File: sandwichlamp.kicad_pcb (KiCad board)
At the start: 2 copper layers, 96 x 96 mm, 17 parts, among them J1 Pole1, J2 Pole2, J3 Pole3, J4 12V Enable, J5 HLK-LD2410C, SW1 Rader Power, SW3 POWER, U1 magnetic-charger, U3 hw357, U4 RX480E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

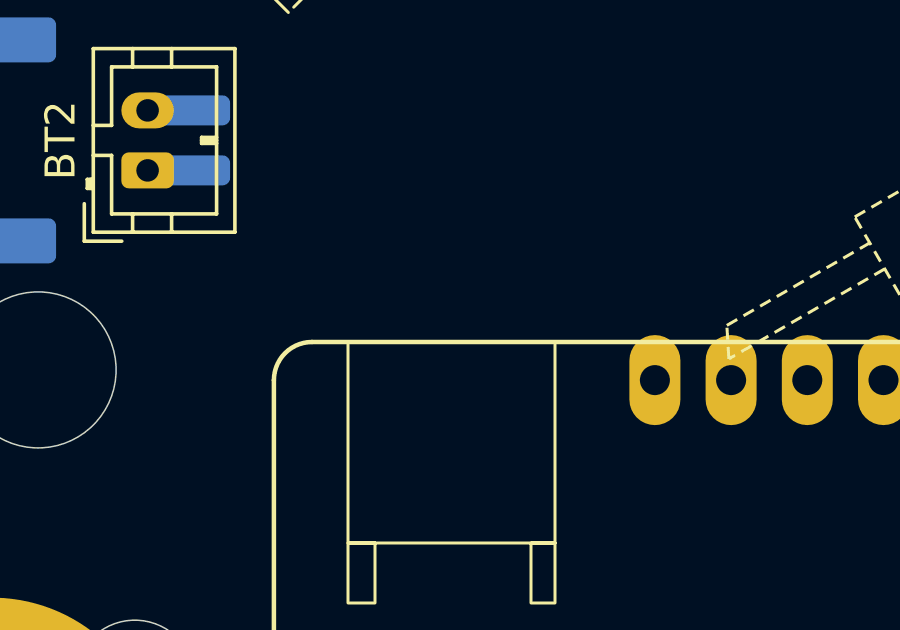
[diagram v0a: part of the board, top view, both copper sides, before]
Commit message: Add battery pad to the Lolin where the battery voltage can be taken for the ESP
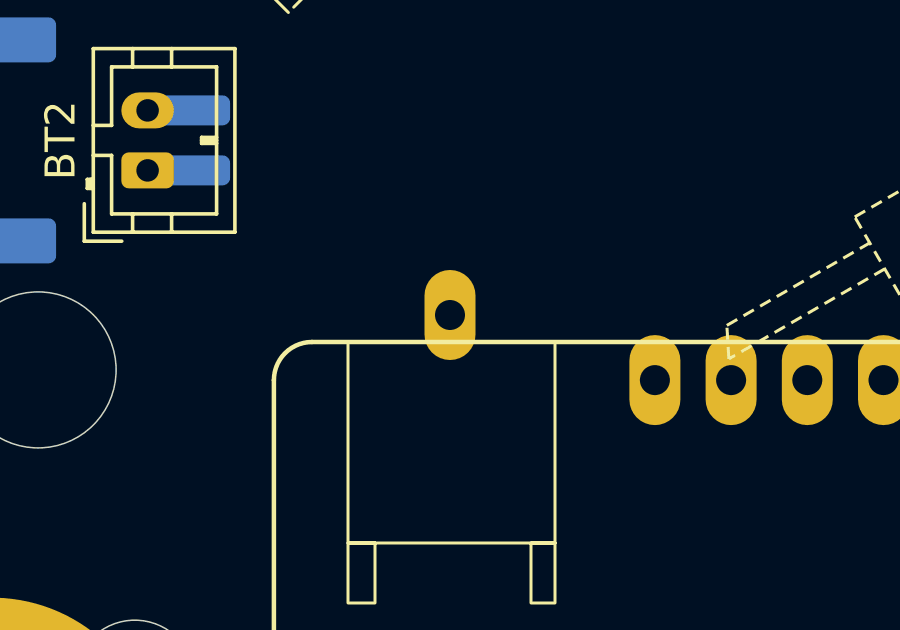
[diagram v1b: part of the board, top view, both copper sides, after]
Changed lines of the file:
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@@
 			(pintype "bidirectional")
+		)
+		(pad "37" thru_hole oval
+			(at -13.6 20.8 270)
+			(size 3 1.7)
+			(drill 1)
+			(layers "*.Cu" "*.Mask")
+			(remove_unused_layers no)
 		)
 		(model "${KIPRJMOD}/lib/lolin32/lolin32.step"

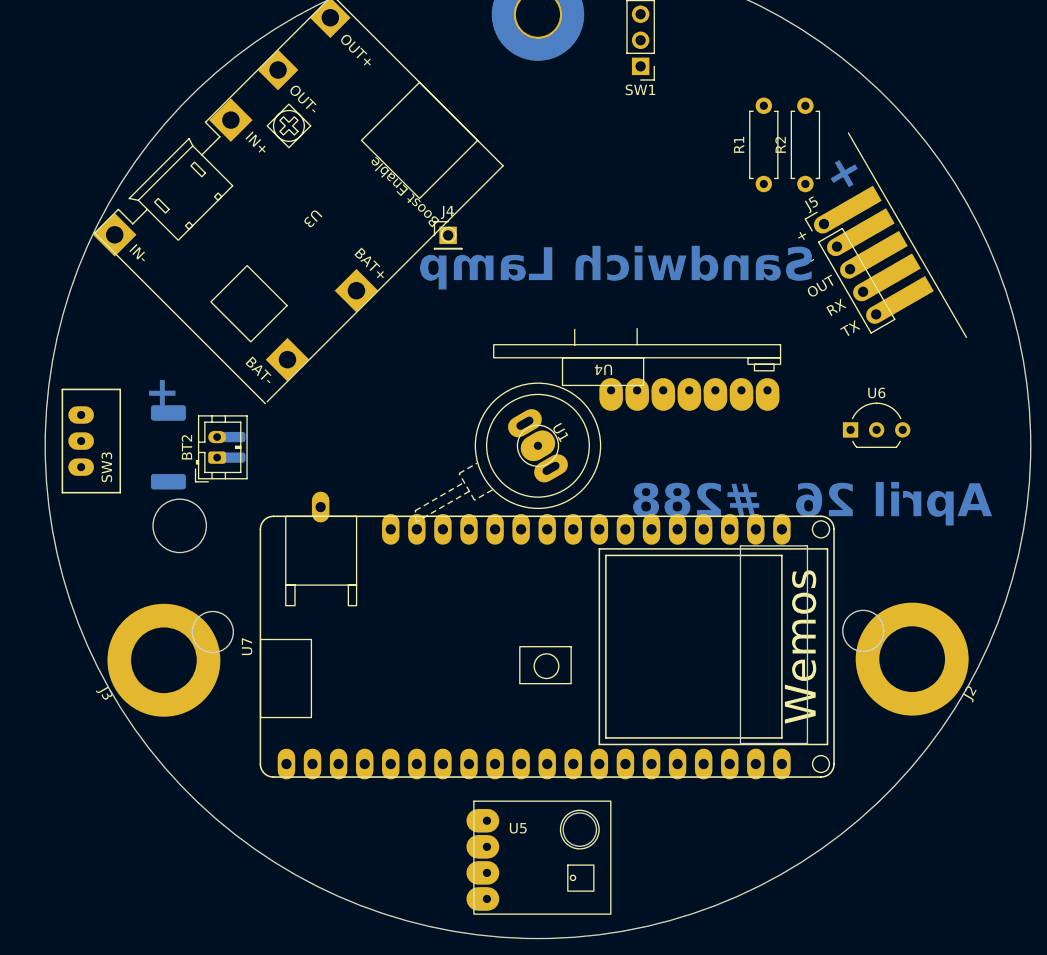
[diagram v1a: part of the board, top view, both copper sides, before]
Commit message: Add M3 mounting holes
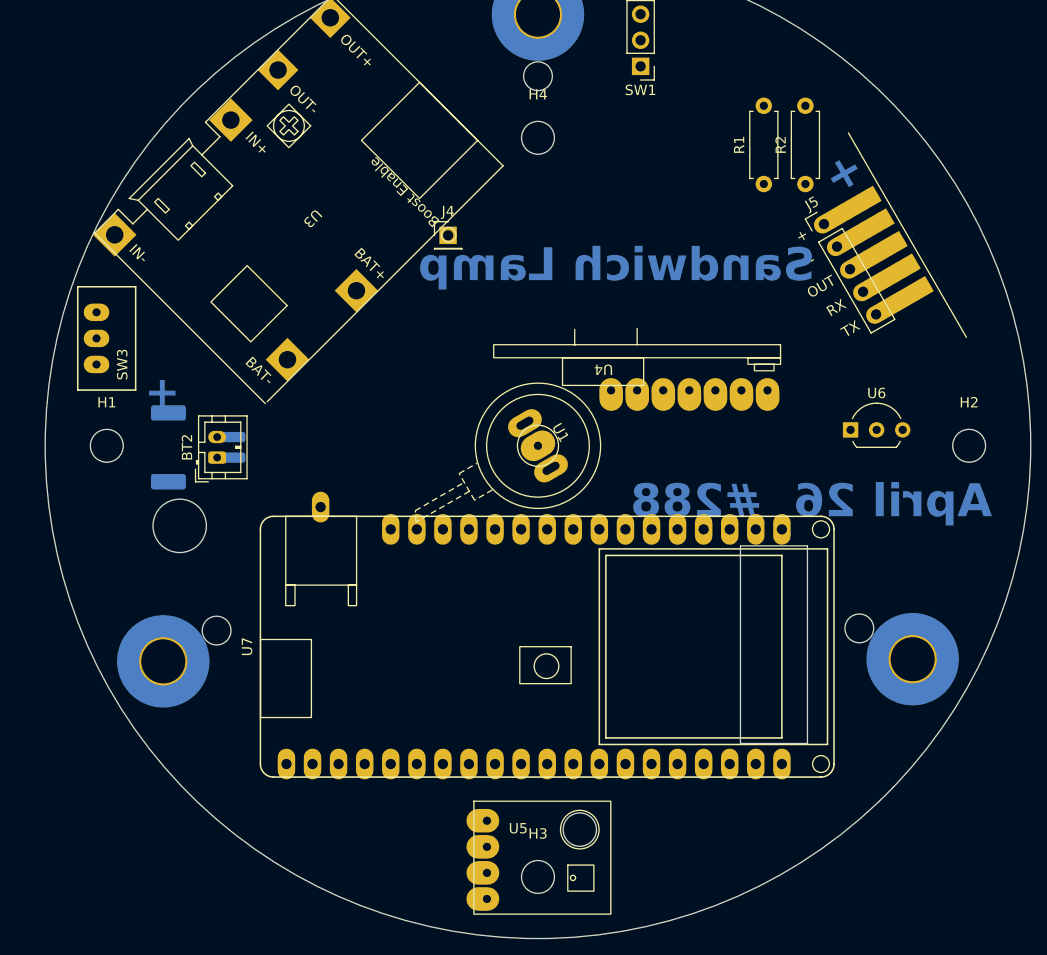
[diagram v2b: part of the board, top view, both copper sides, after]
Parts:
- added H1: MountingHole, MountingHole:MountingHole_3.2mm_M3, F.Cu at (58.0, 100.0)
- added H2: MountingHole, MountingHole:MountingHole_3.2mm_M3, F.Cu at (142.0, 100.0)
- added H3: MountingHole, MountingHole:MountingHole_3.2mm_M3, F.Cu at (100.0, 142.0)
- added H4: MountingHole, MountingHole:MountingHole_3.2mm_M3, F.Cu at (100.0, 70.0)
- J2, J3: footprint MountingHole:MountingHole_6.4mm_M6_DIN965_Pad -> MountingHole:MountingHole_4.3mm_M4_ISO7380_Pad_TopOnly; moved to B.Cu
- moved SW3 10.1 mm to (57.0, 87.0)
- moved J3 0.12 mm to (63.5, 121.0), turned to -60 degrees
- turned J2 to 60 degrees
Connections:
- BT1 pad 1: +4V -> Net-(BT1-+)
- BT2 pad 1: +4V -> Net-(BT1-+)
- SW3 pad 1: unconnected-(SW3-A-Pad1) -> Net-(BT1-+)
- SW3 pad 2: unconnected-(SW3-B-Pad2) -> +4V
- U1 pad 1: unconnected-(U1-GND-Pad1) -> GND
- U1 pad 2: unconnected-(U1-VCC-Pad2) -> VBUS
- U3 pad 5: +4V -> Net-(BT1-+)
- U7 pad 37: (no net) -> +4V

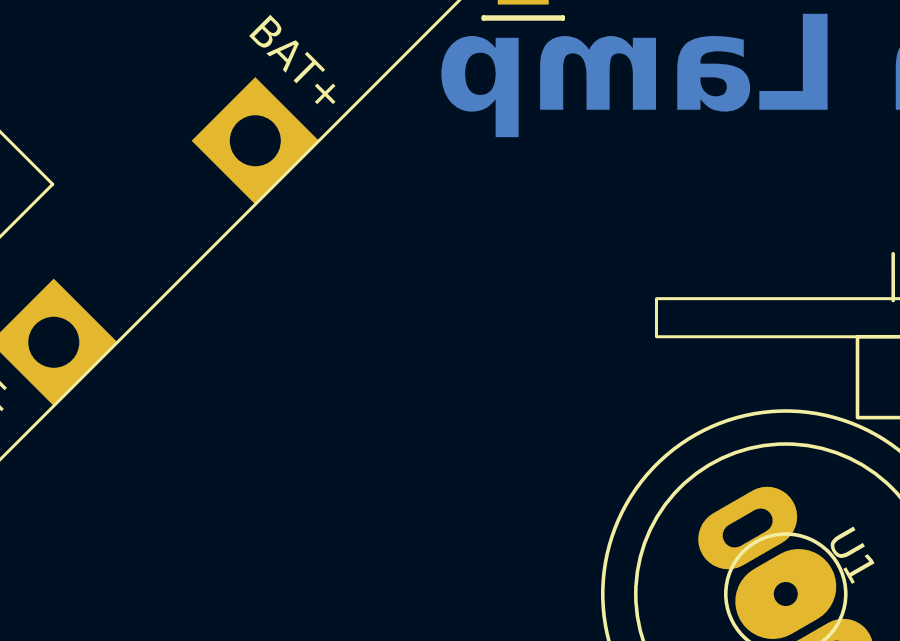
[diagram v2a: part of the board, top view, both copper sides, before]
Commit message: Add a light sensor and the labels for the existing components
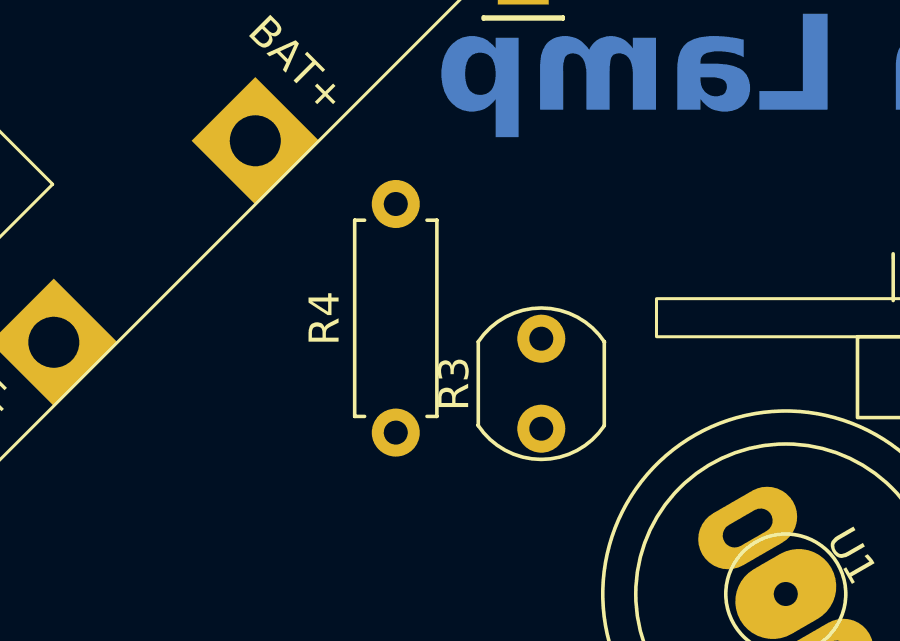
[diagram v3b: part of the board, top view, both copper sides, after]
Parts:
- added R3: R_Photo, OptoDevice:R_LDR_5.0x4.1mm_P3mm_Vertical, F.Cu at (91.8, 94.5)
- added R4: 10k, Resistor_THT:R_Axial_DIN0207_L6.3mm_D2.5mm_P7.62mm_Horizontal, F.Cu at (87.0, 94.6)
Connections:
- net RADAR_RX renamed Radar_RX
- net RADAR_TX renamed Radar_TX
- J1 pad 1: unconnected-(J1-Pin_1-Pad1) -> Touch1
- J2 pad 1: unconnected-(J2-Pin_1-Pad1) -> Touch2
- J3 pad 1: unconnected-(J3-Pin_1-Pad1) -> Touch3
- J4 pad 1: unconnected-(J4-Pin_1-Pad1) -> Enable12V
- U4 pad 2: unconnected-(U4-VCC-Pad2) -> +4V
- U5 pad 1: unconnected-(U5-VIN-Pad1) -> +3V3
- U5 pad 2: unconnected-(U5-GND-Pad2) -> GND
- U5 pad 3: unconnected-(U5-SCL-Pad3) -> SCL
- U5 pad 4: unconnected-(U5-SDA-Pad4) -> SDA

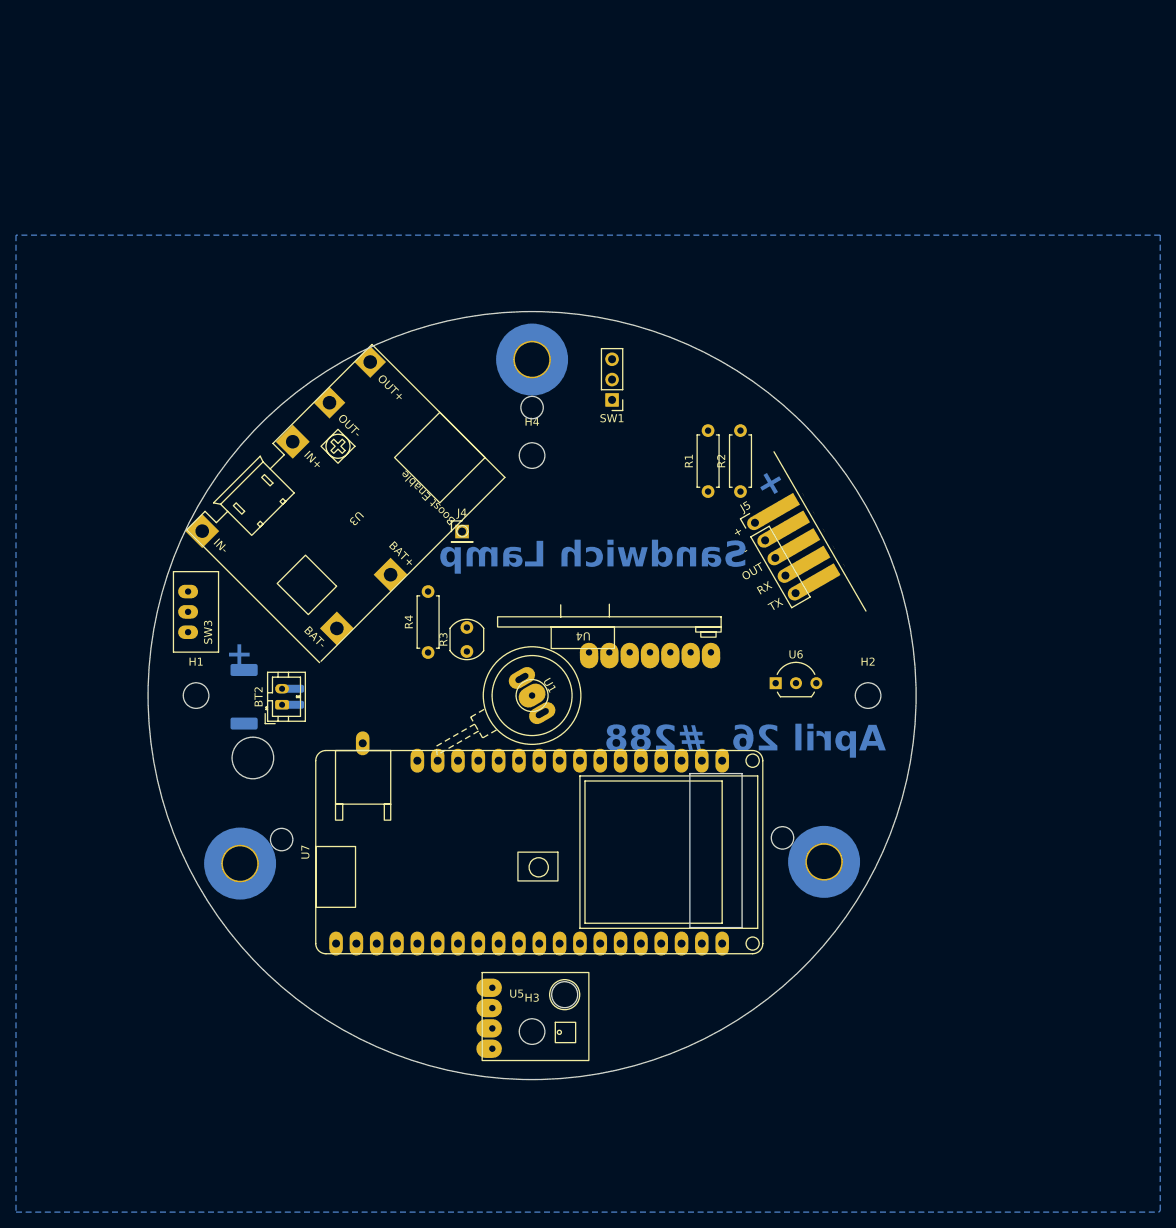
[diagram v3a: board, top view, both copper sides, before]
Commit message: Add Neopixel footprint and do the preliminary routing
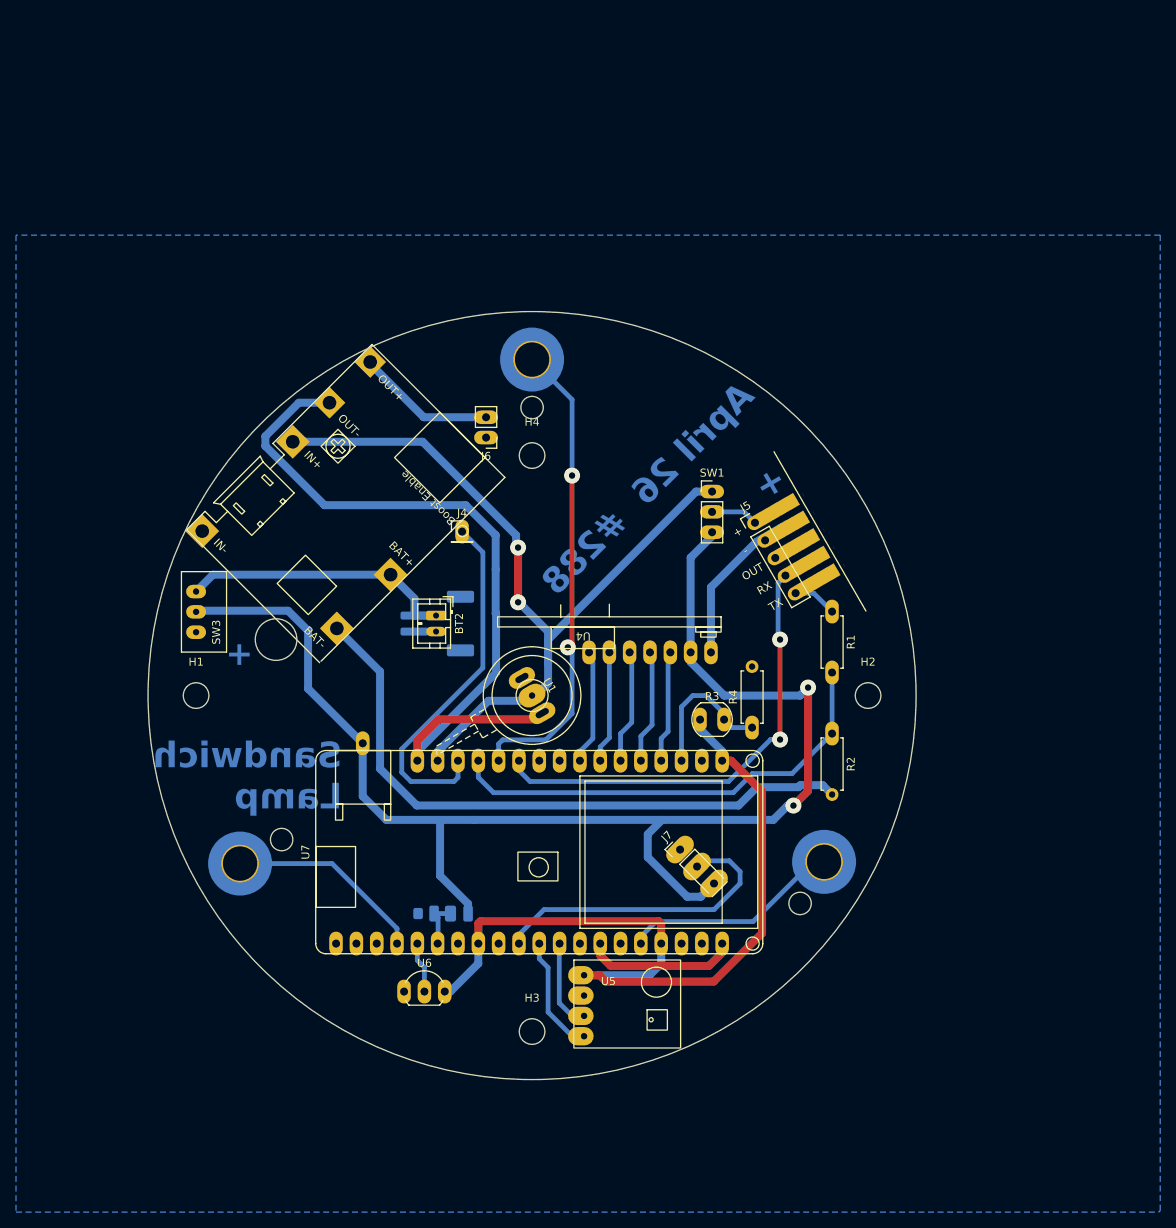
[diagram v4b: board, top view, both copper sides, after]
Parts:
- added J6: Conn_01x02, Connector_PinHeader_2.54mm:PinHeader_1x02_P2.54mm_Vertical, F.Cu at (94.2, 67.8)
- added J7: Conn_01x03, Connector_PinHeader_2.54mm:PinHeader_1x03_P2.54mm_Vertical, F.Cu at (118.5, 119.2)
- added R5: 10k, Resistor_SMD:R_0805_2012Metric_Pad1.20x1.40mm_HandSolder, B.Cu at (86.8, 127.2)
- added R6: 10k, Resistor_SMD:R_0805_2012Metric_Pad1.20x1.40mm_HandSolder, B.Cu at (91.0, 127.2)
- moved U6 60.4 mm to (84.0, 137.0)
- moved R4 41.6 mm to (127.5, 104.0)
- moved R2 32.3 mm to (137.5, 104.8), turned to -90 degrees
- moved R3 30.4 mm to (121.0, 103.0), turned to 0 degrees
- moved BT1 23.1 mm to (88.2, 91.0), turned to -90 degrees
- moved BT2 22.2 mm to (88.0, 90.0), turned to -90 degrees
- moved R1 21.6 mm to (137.5, 89.5), turned to -90 degrees
- moved SW1 17.0 mm to (122.5, 74.5), turned to 0 degrees
- moved U5 11.6 mm to (106.5, 138.8)
- moved SW3 1.00 mm to (58.0, 87.0)
- turned J2 to 150 degrees
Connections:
- net Net-(BT1-+) renamed VBAT
- net Net-(J5-Pin_1) renamed VRadar
- U1 pad 2: VBUS -> +5V
- U3 pad 1: VBUS -> +5V
- U4 pad 1: unconnected-(U4-GND-Pad1) -> GND
- U4 pad 3: unconnected-(U4-D-Pad3) -> Button4
- U4 pad 4: unconnected-(U4-C-Pad4) -> Button3
- U4 pad 5: unconnected-(U4-B-Pad5) -> Button2
- U4 pad 6: unconnected-(U4-A-Pad6) -> Button1
- U4 pad 7: unconnected-(U4-VT-Pad7) -> ButtonX
- U6 pad 1: unconnected-(U6-GND-Pad1) -> GND
- U6 pad 2: unconnected-(U6-DQ-Pad2) -> OneWire
- U6 pad 3: unconnected-(U6-V_{DD}-Pad3) -> +3V3
- U7 pad 11: unconnected-(U7-27-Pad11) -> Radar_TX
- U7 pad 12: unconnected-(U7-14-Pad12) -> Touch1
- U7 pad 13: unconnected-(U7-12-Pad13) -> Radar_RX
- U7 pad 14: unconnected-(U7-13-Pad14) -> Enable12V
- U7 pad 15: VBUS -> +5V
- U7 pad 17: unconnected-(U7-GND-Pad17) -> GND
- U7 pad 21: unconnected-(U7-SCL/22-Pad21) -> Touch2
- U7 pad 25: unconnected-(U7-MISO/19-Pad25) -> SCL
- U7 pad 26: unconnected-(U7-MOSI/23-Pad26) -> SDA
- U7 pad 27: unconnected-(U7-SCK/18-Pad27) -> Neopixel
- U7 pad 3: unconnected-(U7-36/VP-Pad3) -> Brightness
- U7 pad 31: unconnected-(U7-16-Pad31) -> BatterySens
- U7 pad 32: unconnected-(U7-4-Pad32) -> OneWire
- U7 pad 33: unconnected-(U7-0-Pad33) -> Touch3
- U7 pad 4: unconnected-(U7-39/VN-Pad4) -> Button4
- U7 pad 5: unconnected-(U7-32-Pad5) -> Button3
- U7 pad 6: unconnected-(U7-33-Pad6) -> Button2
- U7 pad 7: unconnected-(U7-34-Pad7) -> Button1
- U7 pad 8: unconnected-(U7-35-Pad8) -> ButtonX
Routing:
- net GND: track 0.00 -> 215.6 mm
- net +4V: track 0.00 -> 173.7 mm, vias 0 -> 2
- net +3V3: track 0.00 -> 104.7 mm
- net +5V: track 0.00 -> 102.6 mm, vias 0 -> 2
- net Touch1: track 0.00 -> 59.6 mm, vias 0 -> 2
- net Radar_RX: track 0.00 -> 57.8 mm
- net Radar_TX: track 0.00 -> 57.6 mm, vias 0 -> 2
- net Enable12V: track 0.00 -> 45.2 mm
- net Neopixel: track 0.00 -> 39.1 mm
- net VBAT: track 0.00 -> 34.2 mm
- net Touch2: track 0.00 -> 27.6 mm
- net Touch3: track 0.00 -> 24.9 mm
- net Brightness: track 0.00 -> 18.2 mm
- net +12V: track 0.00 -> 17.5 mm
- net SDA: track 0.00 -> 14.8 mm
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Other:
- outline, holes or cut-outs redrawn

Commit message: Routing
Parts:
- moved H1 12.0 mm to (70.0, 100.0)
- moved H2 12.0 mm to (130.0, 100.0)
- moved R1 8.51 mm to (144.0, 95.0)
- moved R2 1.24 mm to (138.0, 103.6)
- moved R4 0.98 mm to (127.5, 105.0), turned to 0 degrees
- turned U1 to -90 degrees
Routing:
- net GND: track 215.6 -> 290.8 mm
- net +4V: track 173.7 -> 187.3 mm
- net Net-(J5-Pin_5): track 5.51 -> 14.3 mm
- net Radar_TX: track 57.6 -> 62.8 mm
- net +5V: track 102.6 -> 100.3 mm
- net Radar_RX: track 57.8 -> 59.3 mm
- net Neopixel: track 39.1 -> 39.7 mm
- net Touch1: track 59.6 -> 59.8 mm, vias 2 -> 0
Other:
- outline, holes or cut-outs redrawn
